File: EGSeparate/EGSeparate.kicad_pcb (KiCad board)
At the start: 2 copper layers, 100 x 45 mm, 20 parts, among them IC1 PIC16F15325-I_P, IC2 MCP6232-E_P, IC3 2MS1T1B4VS2QES, J1 ICSP, J2 D_Power, J4 Conn_01x04, J5 Conn_01x03

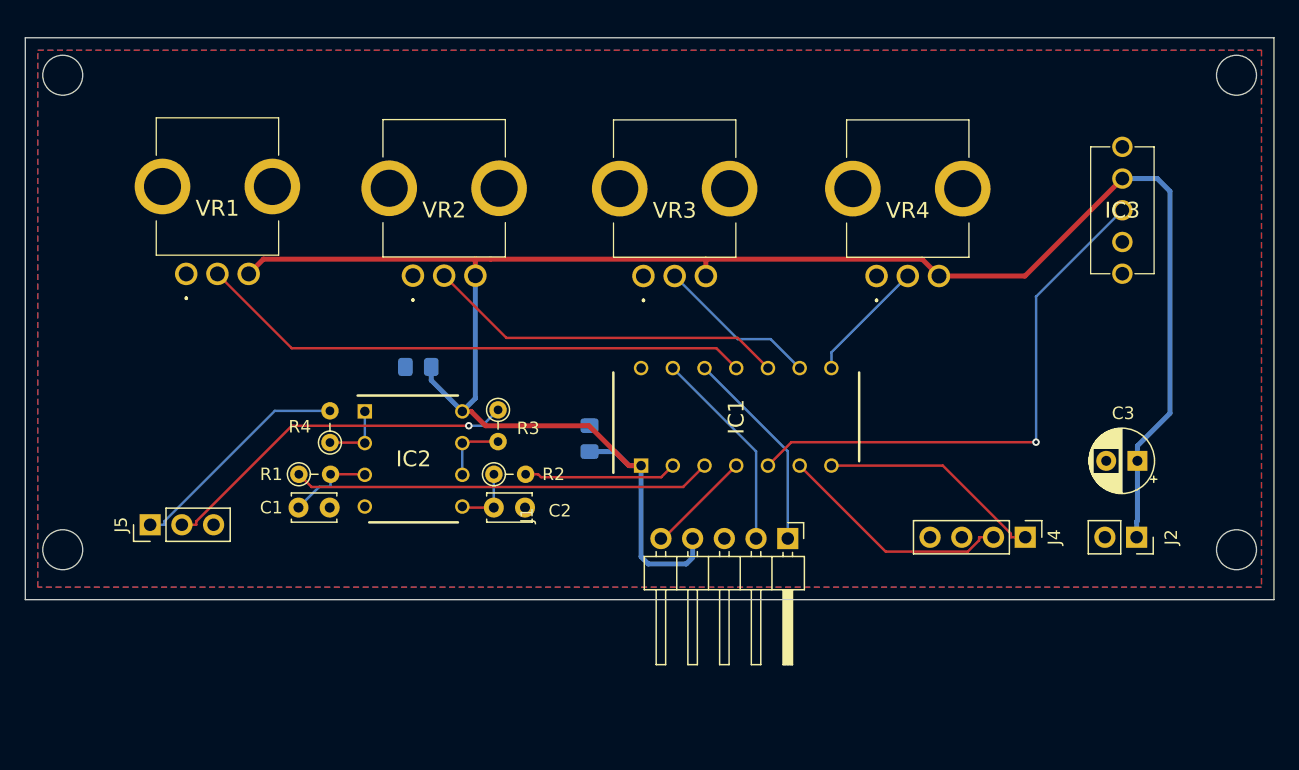
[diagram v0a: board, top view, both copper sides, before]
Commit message: EGSeparate
シルクスクリーンに説明文を追記
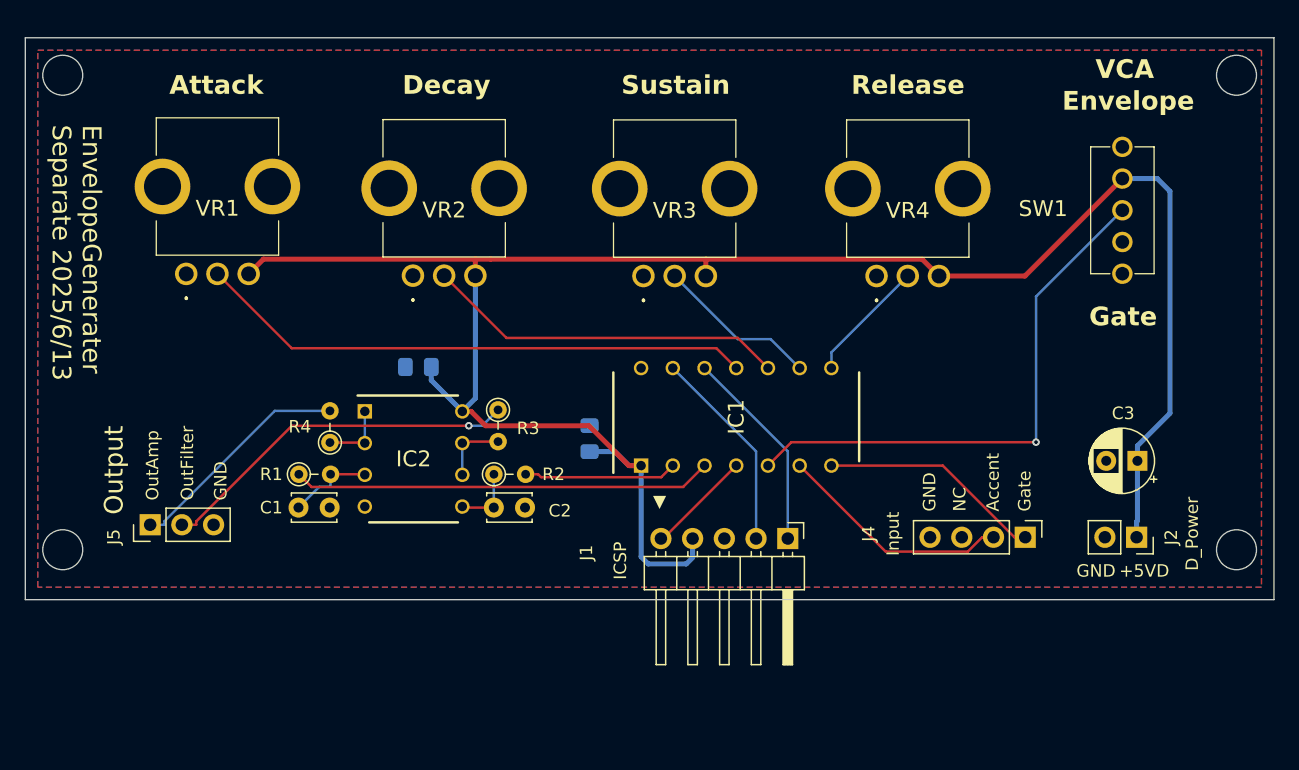
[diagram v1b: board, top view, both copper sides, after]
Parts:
- renumbered IC3 to SW1
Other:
- board text added: "+5VD"
- board text added: "Accent"
- board text added: "Attack"
- board text added: "D_Power"
- board text added: "Decay"
- board text added: "Envelope"
- board text added: "EnvelopeGenerater Separate 2025/6/13"
- board text added: "GND"
- board text added: "Gate"
- board text added: "ICSP"
- board text added: "Input"
- board text added: "NC"
- board text added: "OutAmp"
- board text added: "OutFilter"
- board text added: "Output"
- board text added: "Release"
- board text added: "Sustain"
- board text added: "VCA"
- board text added: "▼"

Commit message: MC2
アクセントレベルを追加したEGACCを登録
回路全般部品配置済
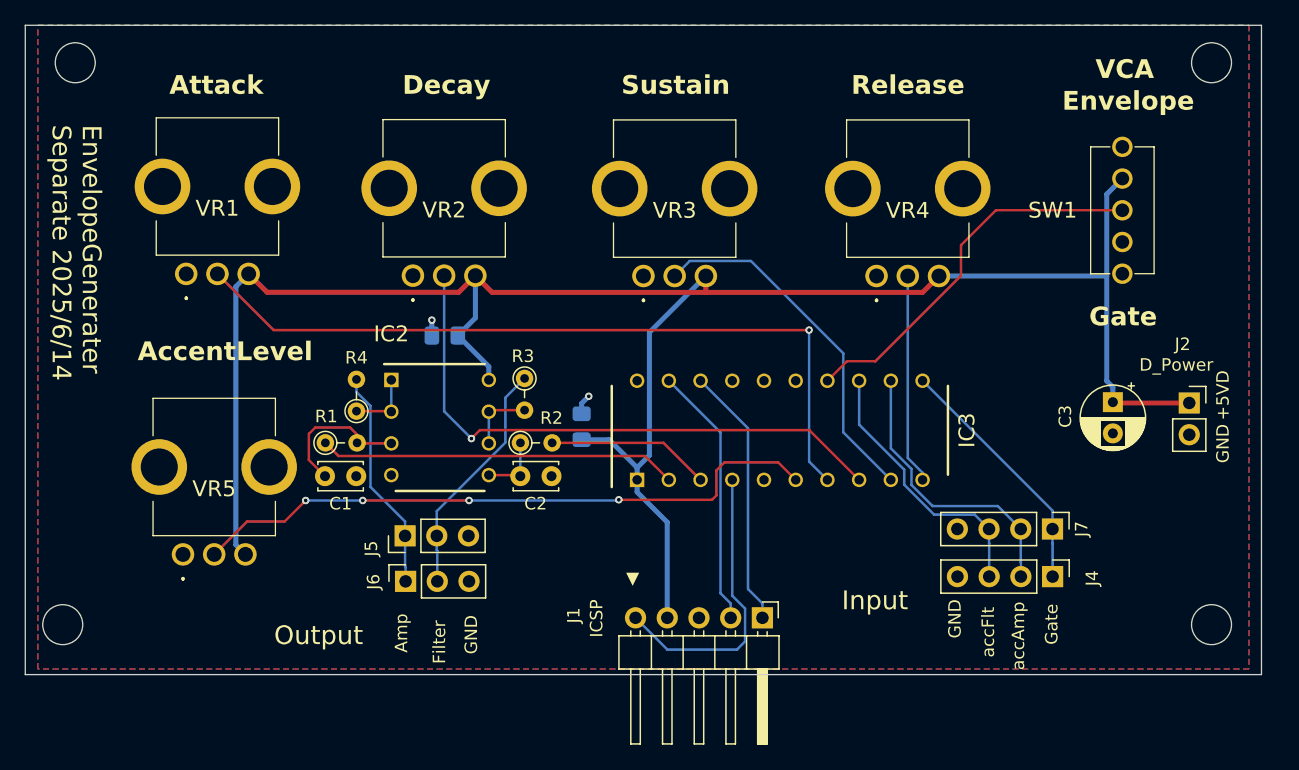
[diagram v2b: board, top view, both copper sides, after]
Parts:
- removed IC1: PIC16F15325-I_P, SamacSys_Parts:DIP781W56P254L1918H533Q14N
- added IC3: PIC16F13145-I_P, SamacSys_Parts:DIP794W56P254L2591H533Q20N, F.Cu at (130.4, 61.4)
- added J6: Conn_01x03, Connector_PinSocket_2.54mm:PinSocket_1x03_P2.54mm_Vertical, F.Cu at (100.5, 73.5)
- added J7: Conn_01x04, Connector_PinHeader_2.54mm:PinHeader_1x04_P2.54mm_Vertical, F.Cu at (152.3, 69.3)
- added VR5: AccLevel 10KB, SamacSys_Parts:RK09D117000B, F.Cu at (82.6, 71.4)
- moved J5 20.4 mm to (100.4, 69.9)
- moved J2 11.5 mm to (163.2, 59.2), turned to 0 degrees
- moved J1 6.67 mm to (129.0, 76.5)
- moved C3 5.09 mm to (157.1, 59.2), turned to -90 degrees
- moved J4 3.84 mm to (152.3, 73.2)
- moved C2 3.29 mm to (109.6, 65.1)
- moved C5 3.29 mm to (103.6, 53.8)
- moved IC2 3.29 mm to (103.2, 61.2)
- moved R3 3.29 mm to (110.0, 57.3)
- moved R4 3.29 mm to (96.5, 59.9)
- moved C1 3.29 mm to (94.0, 65.1)
- moved R1 3.29 mm to (94.0, 62.4)
- moved R2 3.29 mm to (109.7, 62.4)
- moved C4 1.15 mm to (114.6, 61.1)
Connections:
- J4 pad 2: Accent -> accAmp
- J4 pad 3: unconnected-(J4-Pin_3-Pad3) -> accFlt
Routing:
- net AccLv: track 0.00 -> 51.5 mm, vias 0 -> 4
- net accAmp: track 0.00 -> 23.1 mm
- net accFlt: track 0.00 -> 21.9 mm
- net Accent: track 18.9 -> 0.00 mm
- net Decay: track 29.0 -> 46.9 mm, vias 0 -> 1
- net Attack: track 44.7 -> 61.8 mm, vias 0 -> 1
- net Sustain: track 13.1 -> 28.8 mm
- net ~MCLR: track 8.45 -> 23.5 mm
- net AmpWave: track 43.7 -> 30.7 mm, vias 1 -> 0
- net outFlt: track 29.3 -> 19.2 mm, vias 1 -> 0
- net Release: track 9.91 -> 16.8 mm
- net +5VD: track 160.0 -> 166.3 mm
- net PWM_outAmp: track 33.6 -> 28.7 mm
- net Net-(IC2-VINA+): track 7.02 -> 11.7 mm
- net ICSPDT: track 16.4 -> 21.0 mm
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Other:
- board size 100 x 45 mm -> 99 x 52 mm
- board text added: "AccentLevel"
- board text added: "Amp"
- board text added: "EnvelopeGenerater Separate 2025/6/14"
- board text added: "Filter"
- board text added: "accAmp"
- board text added: "accFlt"
- board text removed: "Accent"
- board text removed: "EnvelopeGenerater Separate 2025/6/13"
- board text removed: "NC"
- board text removed: "OutAmp"
- board text removed: "OutFilter"

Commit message: EGACC MC2
プログラムと回路デバッグ後の修正を反映
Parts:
- added C6: 0.01uF, Capacitor_THT:C_Disc_D3.4mm_W2.1mm_P2.50mm, F.Cu at (113.4, 71.5)
- added R5: 1K, Resistor_THT:R_Axial_DIN0204_L3.6mm_D1.6mm_P2.54mm_Vertical, F.Cu at (116.0, 69.1)
- added R6: 100, Resistor_THT:R_Axial_DIN0204_L3.6mm_D1.6mm_P2.54mm_Vertical, F.Cu at (118.3, 71.5)
- IC2: footprint SamacSys_Parts:DIP781W56P254L950H533Q8N -> SamacSys_parts:DIP781W56P254L950H533Q8N
- IC3: footprint SamacSys_Parts:DIP794W56P254L2591H533Q20N -> SamacSys_parts:DIP794W56P254L2591H533Q20N
- SW1: footprint SamacSys_Parts:2MS1T1B4VS2QES -> SamacSys_parts:2MS1T1B4VS2QES
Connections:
- IC3 pad 15: unconnected-(IC3-RC1-Pad15) -> PWM_outAmp
- IC3 pad 2: PWM_outAmp -> unconnected-(IC3-RA5-Pad2)
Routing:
- net PWM_outAmp: track 28.7 -> 40.6 mm
- net Net-(C6-Pad1): track 0.00 -> 6.23 mm
- net ~MCLR: track 23.5 -> 29.0 mm
- net +5VD: track 166.3 -> 170.5 mm
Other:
- board text added: "EnvelopeGenerater Separate Rev2 2025/7/21"
- board text removed: "EnvelopeGenerater Separate 2025/6/14"
